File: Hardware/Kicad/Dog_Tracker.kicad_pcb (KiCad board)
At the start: 2 copper layers, 19 parts, among them IC1 M4 Feather, U1 ADP160AUJZ-1.8-R7, U3 Origin_GPS1510, U4 NFA18SL407V1A45L, U5 SN74AUP1T97, U6 LSM6DSO32

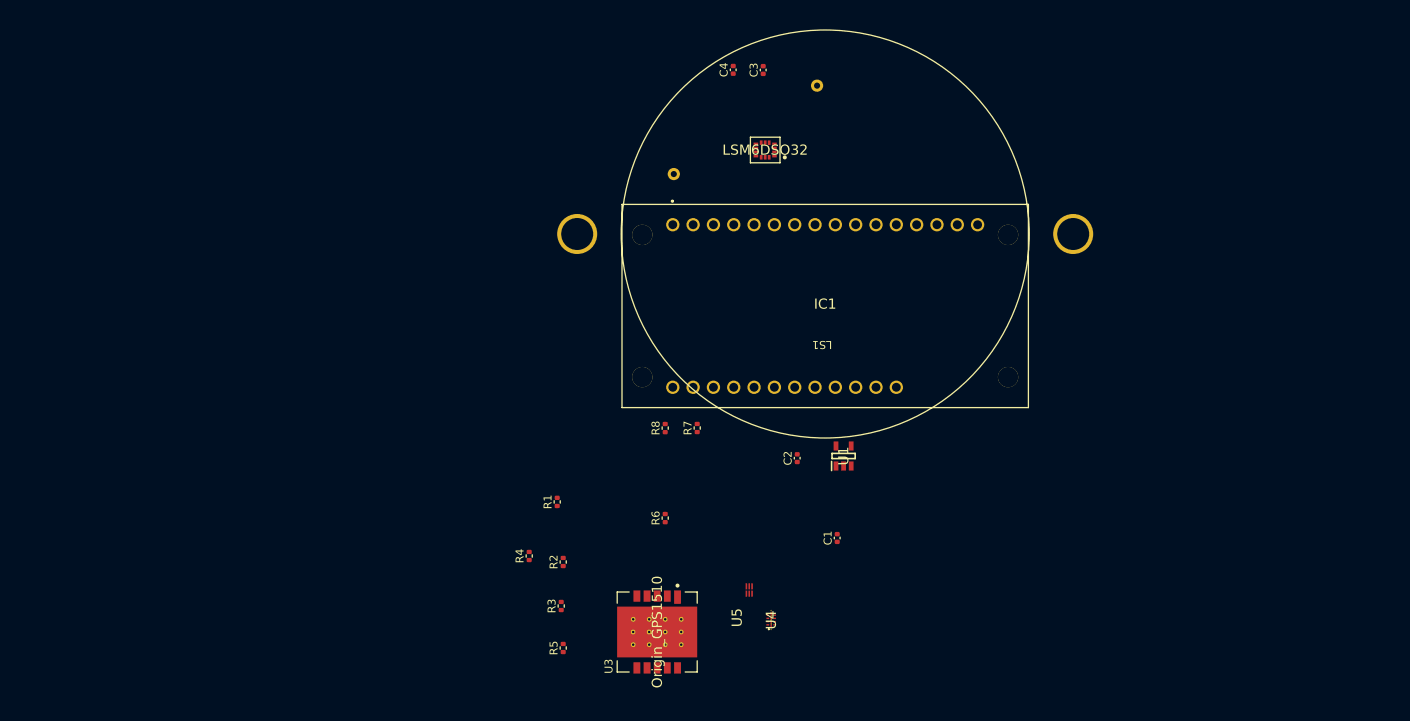
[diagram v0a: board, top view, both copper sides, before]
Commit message: fixed all footprint and added SX1280
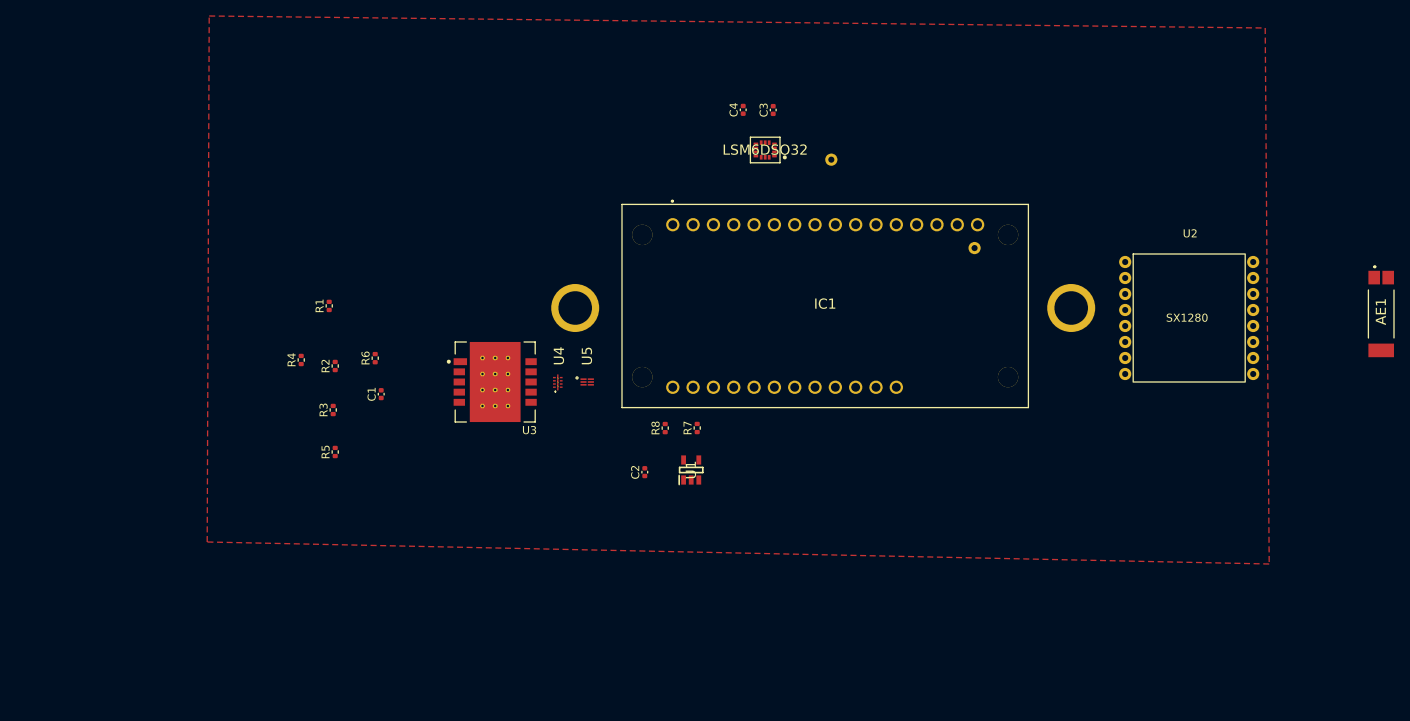
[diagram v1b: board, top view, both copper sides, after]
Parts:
- added AE1: W3211, Dog_Tracker:W3211, F.Cu at (205.8, 99.5)
- added U2: SX1280IMLTRT, Dog_Tracker:SX1280_Breakout, F.Cu at (181.8, 100.0)
- LS1: moved to B.Cu
- moved C1 59.8 mm to (80.8, 109.5)
- moved R6 41.4 mm to (80.0, 105.0)
- moved U4 39.9 mm to (102.8, 108.0)
- moved R1 37.6 mm to (74.2, 98.5)
- moved R2 37.6 mm to (75.0, 106.0)
- moved R3 37.6 mm to (74.8, 111.5)
- moved R4 37.6 mm to (70.8, 105.2)
- moved R5 37.6 mm to (75.0, 116.8)
- moved U3 37.2 mm to (95.0, 108.0), turned to 180 degrees
- moved U5 33.0 mm to (106.5, 108.0), turned to 0 degrees
- moved U1 19.1 mm to (119.5, 119.0)
- moved C2 19.1 mm to (113.7, 119.3)
- moved LS1 9.25 mm to (136.0, 98.8), turned to 0 degrees
- moved C3 5.15 mm to (129.8, 74.0)
- moved C4 5.15 mm to (126.0, 74.0)
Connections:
- U4 pad 10: (no net) -> /I2C_SDA
- U4 pad 3: (no net) -> Net-(R3-Pad1)
- U4 pad 4: (no net) -> Net-(R4-Pad1)
- U4 pad 5: (no net) -> Net-(R5-Pad1)
- U4 pad 6: (no net) -> Net-(R6-Pad1)
- U4 pad 7: (no net) -> unconnected-(U4-Pad7)
- U4 pad 8: (no net) -> unconnected-(U4-Pad8)
- U4 pad 9: (no net) -> Net-(U4-Pad9)
- U5 pad 1: Net-(U4-Pad) -> Net-(U4-Pad9)
- U5 pad 3: Net-(U4-Pad) -> Net-(U4-Pad9)
- U5 pad 6: Net-(U4-Pad) -> Net-(U4-Pad9)
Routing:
- added copper zone on F.Cu, net GND

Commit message: 'remove emi filter and use caps'
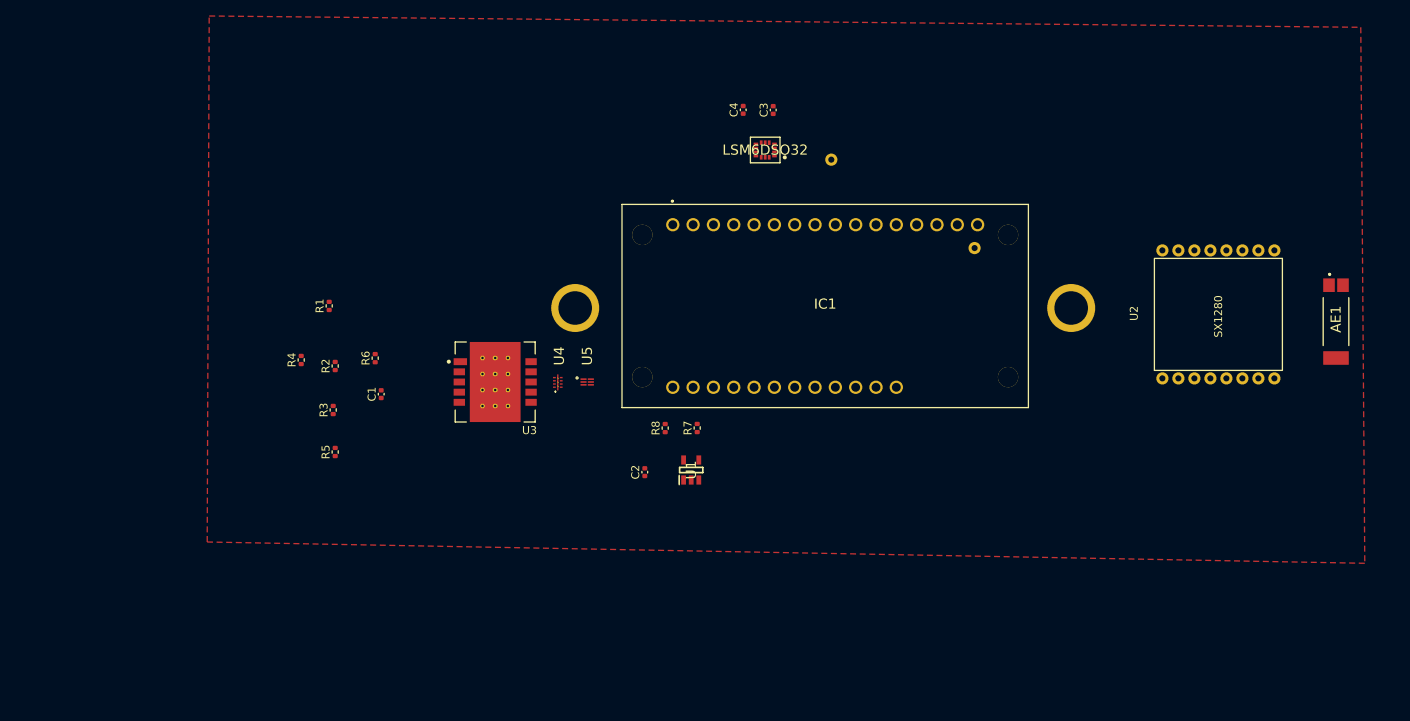
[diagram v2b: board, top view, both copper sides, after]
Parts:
- moved AE1 5.73 mm to (200.1, 100.5)
- moved U2 3.68 mm to (185.4, 99.5), turned to 90 degrees
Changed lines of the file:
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@@
   )
   (footprint "Dog_Tracker:SX1280_Breakout" (layer "F.Cu")
-    (at 181.75 100)
+    (at 185.4 99.55 90)
     (property "Sheetfile" "Dog_Tracker.kicad_sch")
     (property "Sheetname" "")
     (attr through_hole)
-    (fp_text reference "U2" (at 0.127 -10.541 unlocked) (layer "F.SilkS")
-      (effects (font (size 1 1) (thickness 0.15)))
-    )
-    (fp_text value "SX1280IMLTRT" (at -0.127 -8.89 unlocked) (layer "F.Fab")
-      (effects (font (size 1 1) (thickness 0.15)))
-    )
-    (fp_text user "SX1280" (at -0.254 0 unlocked) (layer "F.SilkS")
-      (effects (font (size 1 1) (thickness 0.15)))
-    )
-    (fp_text user "${REFERENCE}" (at 0.127 -10.414 unlocked) (layer "F.Fab")
+    (fp_text reference "U2" (at 0.127 -10.541 90 unlocked) (layer "F.SilkS")
+      (effects (font (size 1 1) (thickness 0.15)))
+    )
+    (fp_text value "SX1280IMLTRT" (at -0.127 -8.89 90 unlocked) (layer "F.Fab")
+      (effects (font (size 1 1) (thickness 0.15)))
+    )
+    (fp_text user "SX1280" (at -0.254 0 90 unlocked) (layer "F.SilkS")
+      (effects (font (size 1 1) (thickness 0.15)))
+    )
+    (fp_text user "${REFERENCE}" (at 0.127 -10.414 90 unlocked) (layer "F.Fab")
       (effects (font (size 1 1) (thickness 0.15)))
     )
     (fp_rect (start -7 -8) (end 7 8) (layer "F.SilkS") (width 0.12) (fill none))
-    (pad "1" thru_hole circle (at -8 -7) (size 1.524 1.524) (drill 0.762) (layers *.Cu *.Mask)
-      (net 2 "GND") (pinfunction "GND") (pintype "power_in"))
-    (pad "2" thru_hole circle (at -8 -5) (size 1.524 1.524) (drill 0.762) (layers *.Cu *.Mask)
+    (pad "1" thru_hole circle (at -8 -7 90) (size 1.524 1.524) (drill 0.762) (layers *.Cu *.Mask)
+      (net 2 "GND") (pinfunction "GND") (pintype "power_in"))
+    (pad "2" thru_hole circle (at -8 -5 90) (size 1.524 1.524) (drill 0.762) (layers *.Cu *.Mask)
       (net 7 "Net-(IC1-Pad4)") (pinfunction "MISO") (pintype "bidirectional"))
-    (pad "3" thru_hole circle (at -8 -3) (size 1.524 1.524) (drill 0.762) (layers *.Cu *.Mask)
+    (pad "3" thru_hole circle (at -8 -3 90) (size 1.524 1.524) (drill 0.762) (layers *.Cu *.Mask)
       (net 8 "Net-(IC1-Pad5)") (pinfunction "MOSI") (pintype "bidirectional"))
-    (pad "4" thru_hole circle (at -8 -1) (size 1.524 1.524) (drill 0.762) (layers *.Cu *.Mask)
+    (pad "4" thru_hole circle (at -8 -1 90) (size 1.524 1.524) (drill 0.762) (layers *.Cu *.Mask)
       (net 9 "Net-(IC1-Pad6)") (pinfunction "SCK") (pintype "bidirectional"))
-    (pad "5" thru_hole circle (at -8 1) (size 1.524 1.524) (drill 0.762) (layers *.Cu *.Mask)
+    (pad "5" thru_hole circle (at -8 1 90) (size 1.524 1.524) (drill 0.762) (layers *.Cu *.Mask)
       (net 10 "/lora cs") (pinfunction "CS") (pintype "bidirectional"))
-    (pad "6" thru_hole circle (at -8 3) (size 1.524 1.524) (drill 0.762) (layers *.Cu *.Mask)
+    (pad "6" thru_hole circle (at -8 3 90) (size 1.524 1.524) (drill 0.762) (layers *.Cu *.Mask)
       (net 4 "/lora reset") (pinfunction "RST") (pintype "bidirectional"))
-    (pad "7" thru_hole circle (at -8 5) (size 1.524 1.524) (drill 0.762) (layers *.Cu *.Mask)
+    (pad "7" thru_hole circle (at -8 5 90) (size 1.524 1.524) (drill 0.762) (layers *.Cu *.Mask)
       (net 45 "unconnected-(U2-Pad7)") (pinfunction "X") (pintype "bidirectional+no_connect"))
-    (pad "8" thru_hole circle (at -8 7) (size 1.524 1.524) (drill 0.762) (layers *.Cu *.Mask)
-      (net 2 "GND") (pinfunction "GND") (pintype "power_in"))
-    (pad "9" thru_hole circle (at 8 7) (size 1.524 1.524) (drill 0.762) (layers *.Cu *.Mask)
+    (pad "8" thru_hole circle (at -8 7 90) (size 1.524 1.524) (drill 0.762) (layers *.Cu *.Mask)
+      (net 2 "GND") (pinfunction "GND") (pintype "power_in"))
+    (pad "9" thru_hole circle (at 8 7 90) (size 1.524 1.524) (drill 0.762) (layers *.Cu *.Mask)
       (net 44 "Net-(AE1-Pad1)") (pinfunction "ANT") (pintype "bidirectional"))
-    (pad "10" thru_hole circle (at 8 5) (size 1.524 1.524) (drill 0.762) (layers *.Cu *.Mask)
-      (net 2 "GND") (pinfunction "GND") (pintype "power_in"))
-    (pad "11" thru_hole circle (at 8 3) (size 1.524 1.524) (drill 0.762) (layers *.Cu *.Mask)
+    (pad "10" thru_hole circle (at 8 5 90) (size 1.524 1.524) (drill 0.762) (layers *.Cu *.Mask)
+      (net 2 "GND") (pinfunction "GND") (pintype "power_in"))
+    (pad "11" thru_hole circle (at 8 3 90) (size 1.524 1.524) (drill 0.762) (layers *.Cu *.Mask)
       (net 46 "unconnected-(U2-Pad11)") (pinfunction "DIO3") (pintype "bidirectional+no_connect"))
-    (pad "12" thru_hole circle (at 8 1) (size 1.524 1.524) (drill 0.762) (layers *.Cu *.Mask)
+    (pad "12" thru_hole circle (at 8 1 90) (size 1.524 1.524) (drill 0.762) (layers *.Cu *.Mask)
       (net 12 "Net-(IC1-Pad9)") (pinfunction "BSY") (pintype "bidirectional"))
-    (pad "13" thru_hole circle (at 8 -1) (size 1.524 1.524) (drill 0.762) (layers *.Cu *.Mask)
+    (pad "13" thru_hole circle (at 8 -1 90) (size 1.524 1.524) (drill 0.762) (layers *.Cu *.Mask)
       (net 1 "+3V3") (pinfunction "3V3") (pintype "power_in"))
-    (pad "14" thru_hole circle (at 8 -3) (size 1.524 1.524) (drill 0.762) (layers *.Cu *.Mask)
+    (pad "14" thru_hole circle (at 8 -3 90) (size 1.524 1.524) (drill 0.762) (layers *.Cu *.Mask)
       (net 47 "unconnected-(U2-Pad14)") (pinfunction "DIO0") (pintype "bidirectional+no_connect"))
-    (pad "15" thru_hole circle (at 8 -5) (size 1.524 1.524) (drill 0.762) (layers *.Cu *.Mask)
+    (pad "15" thru_hole circle (at 8 -5 90) (size 1.524 1.524) (drill 0.762) (layers *.Cu *.Mask)
       (net 48 "unconnected-(U2-Pad15)") (pinfunction "DIO1") (pintype "bidirectional+no_connect"))
-    (pad "16" thru_hole circle (at 8 -7) (size 1.524 1.524) (drill 0.762) (layers *.Cu *.Mask)
+    (pad "16" thru_hole circle (at 8 -7 90) (size 1.524 1.524) (drill 0.762) (layers *.Cu *.Mask)
       (net 49 "unconnected-(U2-Pad16)") (pinfunction "DIO2") (pintype "bidirectional+no_connect"))
   )
   (footprint "Dog_Tracker:W3211" (layer "F.Cu")
-    (at 205.75 99.5 90)
+    (at 200.1 100.45 90)
     (descr "W3211-1")
     (tags "Antenna")
@@
     (polygon
       (pts
-        (xy 191.25 63.75)
-        (xy 191.75 130.75)
+        (xy 203.198215 63.660834)
+        (xy 203.698215 130.660834)
         (xy 59 128)
         (xy 59.25 62.25)
       )
     )
+  )
+  (zone (net 0) (net_name "") (layers F&B.Cu) (hatch edge 0.508)
+    (connect_pads (clearance 0))
+    (min_thickness 0.254)
+    (keepout (tracks not_allowed) (vias not_allowed) (pads not_allowed ) (copperpour not_allowed) (footprints allowed))
+    (fill (thermal_gap 0.508) (thermal_bridge_width 0.508))
+    (polygon
+      (pts
+        (xy 202.1 94.95)
+        (xy 202.1 105.75)
+        (xy 193.85 105.75)
+        (xy 193.85 94.95)
+      )
+    )

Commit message: pcb check
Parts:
- removed U4: NFA18SL407V1A45L, Dog_Tracker:NFA18SL307V1A45B
- added C5: 22pF, Capacitor_SMD:C_0402_1005Metric, F.Cu at (61.4, 122.0)
- added C6: 22pF, Capacitor_SMD:C_0402_1005Metric, F.Cu at (62.8, 108.8)
- moved AE1 143.7 mm to (57.9, 79.5), turned to 180 degrees
- moved U2 129.9 mm to (55.5, 94.8), turned to 180 degrees
- moved U1 69.1 mm to (50.8, 111.8), turned to -90 degrees
- moved C2 60.8 mm to (53.2, 112.8)
- moved U3 42.2 mm to (54.4, 119.5), turned to 90 degrees
- moved U5 41.7 mm to (64.9, 110.8)
- moved C3 38.8 mm to (92.2, 84.0)
- moved U6 38.0 mm to (91.6, 87.1)
- moved C4 37.1 mm to (90.3, 84.1)
- moved R7 37.0 mm to (83.7, 119.2), turned to -90 degrees
- moved IC1 36.4 mm to (100.2, 103.7)
- moved LS1 36.1 mm to (100.2, 104.1)
- moved R8 35.5 mm to (81.2, 119.2), turned to -90 degrees
- moved R6 30.7 mm to (57.6, 125.9), turned to 0 degrees
- moved C1 29.0 mm to (51.8, 108.6)
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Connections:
- net Net-(AE1-Pad1) renamed /ANT
- net Net-(IC1-Pad4) renamed /MISO
- net Net-(IC1-Pad5) renamed /MOSI
- net Net-(IC1-Pad6) renamed /SCK
- net Net-(IC1-Pad9) renamed /BUSY
- net Net-(R3-Pad1) renamed /CTS
- net Net-(R4-Pad1) renamed /RTS
- R5 pad 1: Net-(R5-Pad1) -> Net-(C6-Pad1)
- R6 pad 1: Net-(R6-Pad1) -> /I2C_SDA
- U3 pad 10: Net-(R6-Pad1) -> /I2C_SDA
- U3 pad 3: Net-(R5-Pad1) -> Net-(C6-Pad1)
- U5 pad 1: Net-(U4-Pad9) -> Net-(C6-Pad1)
- U5 pad 3: Net-(U4-Pad9) -> Net-(C6-Pad1)
- U5 pad 6: Net-(U4-Pad9) -> Net-(C6-Pad1)
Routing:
- net +3V3: track 0.00 -> 177.6 mm, vias 0 -> 8
- net /BUSY: track 0.00 -> 65.5 mm
- net /wakeup: track 0.00 -> 53.0 mm, vias 0 -> 1
- net /gps reset: track 0.00 -> 52.5 mm, vias 0 -> 1
- net /MISO: track 0.00 -> 40.2 mm, vias 0 -> 2
- net /SCK: track 0.00 -> 39.8 mm, vias 0 -> 1
- net +1V8: track 0.00 -> 38.1 mm
- net /MOSI: track 0.00 -> 35.5 mm, vias 0 -> 2
- net /I2C_SDA: track 0.00 -> 32.8 mm
- net GND: track 0.00 -> 27.1 mm, vias 0 -> 18
- net /I2C_SCL: track 0.00 -> 24.7 mm
- net /lora reset: track 0.00 -> 18.4 mm
- net Net-(C6-Pad1): track 0.00 -> 15.7 mm
- net /lora cs: track 0.00 -> 15.3 mm
- net Net-(IC1-Pad11): track 0.00 -> 10.4 mm
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- added copper zone on B.Cu, net (none)
- added copper zone on F.Cu, net (none)
- added copper zone on In2.Cu, net +3V3
- added copper zone on In1.Cu, net GND
- removed copper zone on F.Cu, net GND
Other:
- board outline added: 109 x 53.7 mm
- copper layers 2 -> 4

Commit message: layout done
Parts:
- moved AE1 0.33 mm to (58.0, 79.8)
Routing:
- net /pedometer cs: track 0.00 -> 60.0 mm, vias 0 -> 1
- net /GPS_ON: track 0.00 -> 51.6 mm, vias 0 -> 1
- net /lora cs: track 15.3 -> 34.2 mm
- net GND: track 27.1 -> 37.1 mm, vias 18 -> 23
- net Net-(C6-Pad1): track 15.7 -> 22.0 mm
- net +3V3: track 177.6 -> 179.9 mm
- net /gps reset: track 52.5 -> 50.9 mm
- net +1V8: track 38.1 -> 36.5 mm
- net /I2C_SCL: track 24.7 -> 24.2 mm
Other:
- board text added: "Kylee & Angie's Dawg Tracker"

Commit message: gerbers
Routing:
- net +3V3: track 179.9 -> 181.1 mm
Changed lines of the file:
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@@
   (segment (start 74.4 120.15) (end 76.9 120.15) (width 0.6096) (layer "In2.Cu") (net 1))
   (segment (start 45.55 95.85) (end 53.7 95.85) (width 0.6096) (layer "In2.Cu") (net 1))
+  (segment (start 106.93 120.2) (end 76.95 120.2) (width 0.6096) (layer "In2.Cu") (net 1))
   (segment (start 50.470985 108.455689) (end 52.155689 108.455689) (width 0.6096) (layer "In2.Cu") (net 1))
   (segment (start 61.96 110.45) (end 71.66 120.15) (width 0.6096) (layer "In2.Cu") (net 1))
   (segment (start 81.424463 84.625) (end 89.3625 84.625) (width 0.6096) (layer "In2.Cu") (net 1))
   (segment (start 53.7 95.85) (end 57.1 99.25) (width 0.6096) (layer "In2.Cu") (net 1))
-  (segment (start 116.76 93.74) (end 116.76 108.330537) (width 0.6096) (layer "In2.Cu") (net 1))
   (segment (start 73.113189 116.363189) (end 73.113189 92.936274) (width 0.6096) (layer "In2.Cu") (net 1))
   (segment (start 57.1 110.45) (end 61.96 110.45) (width 0.6096) (layer "In2.Cu") (net 1))
   (segment (start 71.66 120.15) (end 74.4 120.15) (width 0.6096) (layer "In2.Cu") (net 1))
-  (segment (start 104.890537 120.2) (end 76.95 120.2) (width 0.6096) (layer "In2.Cu") (net 1))
   (segment (start 74.4 120.15) (end 74.45 120.2) (width 0.2) (layer "In2.Cu") (net 1))
   (segment (start 76.95 120.2) (end 73.113189 116.363189) (width 0.6096) (layer "In2.Cu") (net 1))
@@
   (segment (start 73.113189 92.936274) (end 81.424463 84.625) (width 0.6096) (layer "In2.Cu") (net 1))
   (segment (start 49.85 109.25) (end 49.85 109.076674) (width 0.6096) (layer "In2.Cu") (net 1))
+  (segment (start 116.76 93.74) (end 116.76 110.37) (width 0.6096) (layer "In2.Cu") (net 1))
+  (segment (start 116.76 110.37) (end 106.93 120.2) (width 0.6096) (layer "In2.Cu") (net 1))
   (segment (start 49.85 109.076674) (end 50.470985 108.455689) (width 0.6096) (layer "In2.Cu") (net 1))
-  (segment (start 116.76 108.330537) (end 104.890537 120.2) (width 0.6096) (layer "In2.Cu") (net 1))
   (segment (start 76.9 120.15) (end 76.95 120.2) (width 0.6096) (layer "In2.Cu") (net 1))
   (segment (start 52.155689 108.455689) (end 52.75 109.05) (width 0.6096) (layer "In2.Cu") (net 1))
